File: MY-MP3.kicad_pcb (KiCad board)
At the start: 4 copper layers, 32.4 x 105.7 mm, 85 parts, among them J1 microSD, J2 USB_C_Receptacle, J3 JST_2mm_LiPo, J4 Adafruit 5393 Headers, J7 AudioJack3_SwitchTR, Q1 DMG3415U, SW1 SMD_6x3.5mm_h2.5mm, SW2 SMD_6x3.5mm_h2.5mm, SW3 BTN_POW, SW4 BTN_VUP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

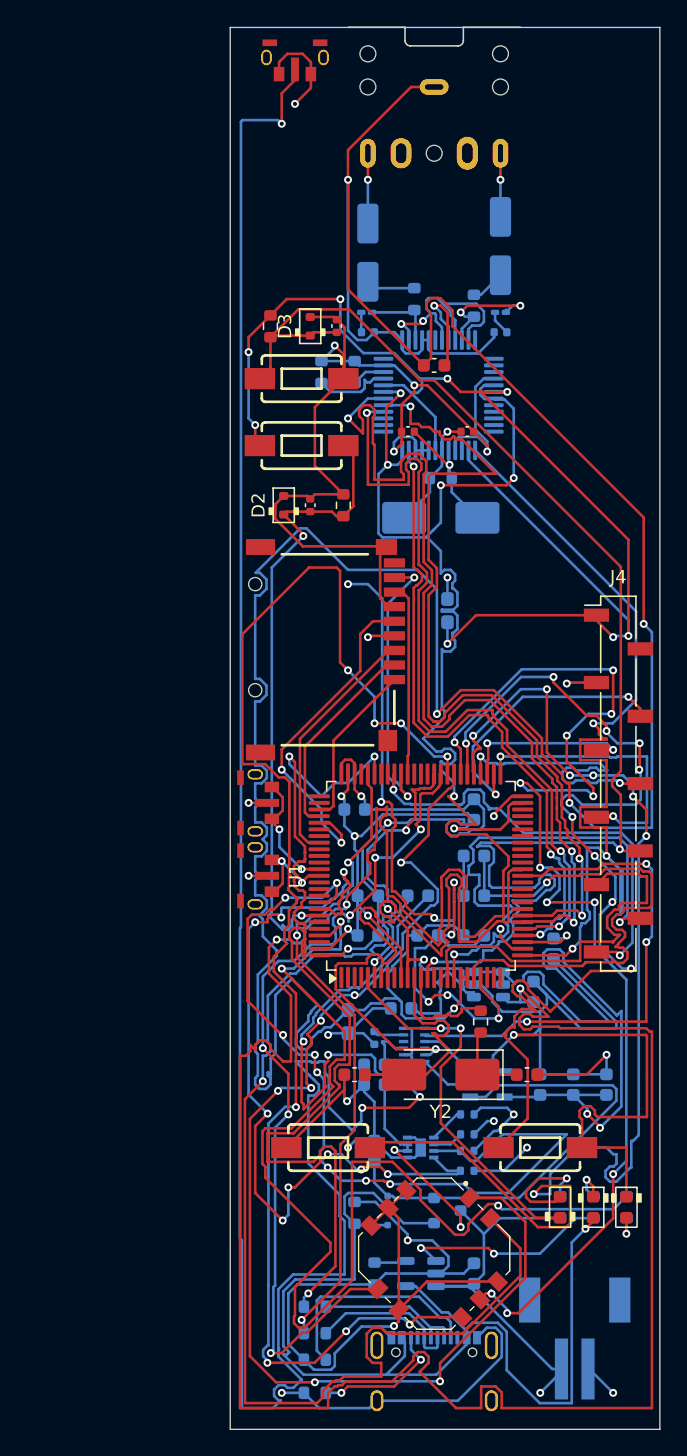
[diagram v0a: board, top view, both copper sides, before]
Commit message: Redo PCB for smaller size and better bin placements
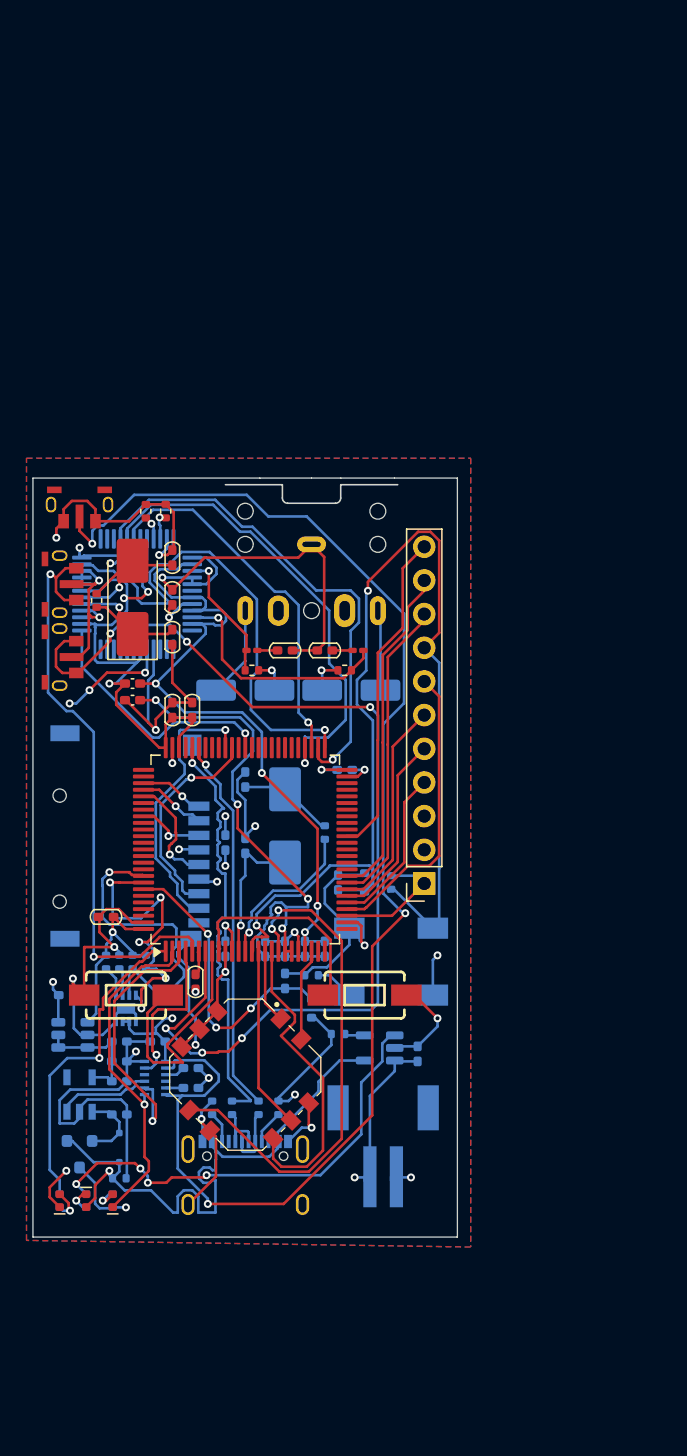
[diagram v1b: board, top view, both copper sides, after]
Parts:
- C1, C14, C16, C17, C2, C20, C21, C22, C23, C25, C26, C27, C29, C3, C30, C6: footprint PCM_SparkFun-Capacitor:C_0603_1608Metric -> PCM_Capacitor_SMD_Handsoldering_AKL:C_0402_1005Metric_Pad0.74x0.62mm
- C11, C13: footprint PCM_SparkFun-Capacitor:C_0603_1608Metric -> PCM_Capacitor_SMD_Handsoldering_AKL:C_0402_1005Metric_Pad0.74x0.62mm; moved to B.Cu
- C12, C18, C19, C31: footprint PCM_SparkFun-Capacitor:C_0603_1608Metric -> PCM_Capacitor_SMD_Handsoldering_AKL:C_0402_1005Metric_Pad0.74x0.62mm; moved to F.Cu
- C15, C24: footprint PCM_SparkFun-Capacitor:C_0402_1005Metric -> PCM_Capacitor_SMD_Handsoldering_AKL:C_0402_1005Metric_Pad0.74x0.62mm; moved to B.Cu
- C28, C4, C5: footprint PCM_SparkFun-Capacitor:C_0402_1005Metric -> PCM_Capacitor_SMD_Handsoldering_AKL:C_0402_1005Metric_Pad0.74x0.62mm
- C7, C8: footprint PCM_SparkFun-Capacitor:C_0402_1005Metric -> PCM_Capacitor_SMD_Handsoldering_AKL:C_0402_1005Metric_Pad0.74x0.62mm; moved to F.Cu
- D2, D3, J1, SW1, SW2, Y2: moved to B.Cu
- FB1, FB2: footprint Inductor_SMD:L_0603_1608Metric_Pad1.05x0.95mm_HandSolder -> Inductor_SMD:L_0402_1005Metric_Pad0.77x0.64mm_HandSolder; moved to F.Cu
- J4: footprint Connector_PinSocket_2.54mm:PinSocket_1x11_P2.54mm_Vertical_SMD_Pin1Left -> Connector_PinSocket_2.54mm:PinSocket_1x11_P2.54mm_Vertical
- LED1: footprint PCM_LED_SMD_AKL:LED_0603_1608Metric -> PCM_SparkFun-LED:LED_0402_1005Metric_Orange
- LED2: footprint PCM_LED_SMD_AKL:LED_0603_1608Metric -> PCM_SparkFun-LED:LED_0402_1005Metric_Green
- LED3: footprint PCM_LED_SMD_AKL:LED_0603_1608Metric -> PCM_SparkFun-LED:LED_0402_1005Metric_Red
- R10, R9, Y1: moved to F.Cu
- R11, R21, R3: footprint PCM_SparkFun-Resistor:R_0603_1608Metric -> PCM_SparkFun-Resistor:R_0402_1005Metric; moved to B.Cu
- R12, R13, R14, R15, R16, R18, R19, R20, R25: footprint PCM_SparkFun-Resistor:R_0603_1608Metric -> PCM_SparkFun-Resistor:R_0402_1005Metric
- R4, R5, R6, R7, R8: footprint PCM_SparkFun-Resistor:R_0603_1608Metric -> PCM_SparkFun-Resistor:R_0402_1005Metric; moved to F.Cu
- moved R21 42.9 mm to (156.8, 102.0)
- moved LED2 42.8 mm to (131.8, 126.0), turned to 90 degrees
- moved R25 42.8 mm to (131.8, 126.0)
- moved D3 42.1 mm to (154.8, 102.0)
- moved SW1 42.0 mm to (156.8, 105.5), turned to 180 degrees
- moved SW2 42.0 mm to (156.8, 110.5), turned to 180 degrees
- moved C15 42.0 mm to (152.8, 102.0)
- moved LED1 38.3 mm to (133.8, 126.0)
- moved R20 38.3 mm to (133.8, 126.0), turned to 90 degrees
- moved D2 38.0 mm to (150.8, 111.5), turned to -90 degrees
- moved SW3 37.4 mm to (133.2, 73.5)
- moved C27 36.9 mm to (136.2, 114.0), turned to 0 degrees
- moved C24 35.9 mm to (148.8, 109.4)
- moved J7 35.7 mm to (150.8, 76.5)
- moved R3 35.5 mm to (150.8, 109.0), turned to 180 degrees
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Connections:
- J4 pad 4: /SPI2_SCK -> /SPI1_SCK
- J4 pad 5: /SPI2_MISO -> /SPI1_MISO
- J4 pad 6: /SPI2_MOSI -> /SPI1_MOSI
- J4 pad 7: /SPI2_NSS -> /SPI1_NSS
- U1 pad 1: unconnected-(U1-PE2-Pad1) -> /LED
- U1 pad 15: /JOY_X -> /BTN_PLAY
- U1 pad 16: /JOY_Y -> /BTN_UP
- U1 pad 17: /TFT_DC -> /BTN_DN
- U1 pad 18: /TFT_SD_CS -> /BTN_TRACK
- U1 pad 2: unconnected-(U1-PE3-Pad2) -> /NVCC_LO
- U1 pad 23: unconnected-(U1-PA0-Pad23) -> /BTN_SEEK
- U1 pad 26: /XDCS -> unconnected-(U1-PA3-Pad26)
- U1 pad 3: unconnected-(U1-PE4-Pad3) -> /NPB_OUT
- U1 pad 33: unconnected-(U1-PC4-Pad33) -> /TFT_DC
- U1 pad 34: unconnected-(U1-PC5-Pad34) -> /TFT_SD_CS
- U1 pad 38: /NPB_OUT -> unconnected-(U1-PE7-Pad38)
- U1 pad 39: /STM6601_NINT -> unconnected-(U1-PE8-Pad39)
- U1 pad 4: unconnected-(U1-PE5-Pad4) -> /STM6601_NINT
- U1 pad 40: unconnected-(U1-PE9-Pad40) -> /TIM1_CH1
- U1 pad 5: /NVCC_LO -> /BTN_VUP
- U1 pad 55: /BTN_OPT -> unconnected-(U1-PD8-Pad55)
- U1 pad 56: /BTN_SEL -> unconnected-(U1-PD9-Pad56)
- U1 pad 57: /BTN_PLAY -> unconnected-(U1-PD10-Pad57)
- U1 pad 58: /BTN_UP -> unconnected-(U1-PD11-Pad58)
- U1 pad 59: /BTN_DN -> unconnected-(U1-PD12-Pad59)
- U1 pad 60: /BTN_TRACK -> unconnected-(U1-PD13-Pad60)
- U1 pad 61: /BTN_SEEK -> unconnected-(U1-PD14-Pad61)
- U1 pad 63: unconnected-(U1-PC6-Pad63) -> /XDCS
- U1 pad 67: /TIM1_CH1 -> unconnected-(U1-PA8-Pad67)
- U1 pad 7: unconnected-(U1-PC13-Pad7) -> /BTN_VDN
- U1 pad 8: unconnected-(U1-PC14-Pad8) -> /BTN_OPT
- U1 pad 87: /BTN_VUP -> unconnected-(U1-PD6-Pad87)
- U1 pad 88: /BTN_VDN -> unconnected-(U1-PD7-Pad88)
- U1 pad 9: unconnected-(U1-PC15-Pad9) -> /BTN_SEL
- U1 pad 97: /LED -> unconnected-(U1-PE0-Pad97)
- U2 pad 23: /SPI1_NSS -> /SPI2_NSS
- U2 pad 28: /SPI1_SCK -> /SPI2_SCK
- U2 pad 29: /SPI1_MOSI -> /SPI2_MOSI
- U2 pad 30: /SPI1_MISO -> /SPI2_MISO
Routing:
- net 1.8V: track 260.8 -> 20.7 mm, vias 8 -> 5
- net GNDA: track 254.5 -> 73.0 mm
- net GND: track 344.7 -> 196.4 mm, vias 24 -> 23
- net 3.3V: track 192.6 -> 81.4 mm, vias 18 -> 10
- net /BTN_SEEK: track 96.8 -> 6.97 mm, vias 2 -> 0
- net /BTN_UP: track 90.7 -> 5.57 mm, vias 7 -> 0
- net /BTN_DN: track 108.0 -> 23.5 mm, vias 8 -> 0
- net /BTN_PLAY: track 90.1 -> 13.8 mm, vias 12 -> 0
- net /BTN_VDN: track 7.40 -> 79.8 mm, vias 2 -> 6
- net /BTN_OPT: track 90.0 -> 18.5 mm, vias 7 -> 0
- net /LED: track 85.8 -> 24.5 mm, vias 3 -> 1
- net /BTN_SEL: track 76.4 -> 16.0 mm, vias 9 -> 0
- net Net-(U5-~{PB}): track 165.4 -> 106.4 mm
- net VBATT: track 82.5 -> 26.6 mm, vias 5 -> 4
- net /SPI1_MISO: track 69.6 -> 14.3 mm, vias 3 -> 0
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- added copper zone on B.Cu, net (none)
- added copper zone on F.Cu, net (none)
- added copper zone on In1.Cu, net 1.8V
- added copper zone on In2.Cu, net GNDA
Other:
- board size 32.4 x 105.7 mm -> 32 x 57.2 mm
